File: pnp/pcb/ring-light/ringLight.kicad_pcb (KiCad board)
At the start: 2 copper layers, 40 x 50.2 mm, 33 parts, among them J1 Connector Top, J2 Connector Bot

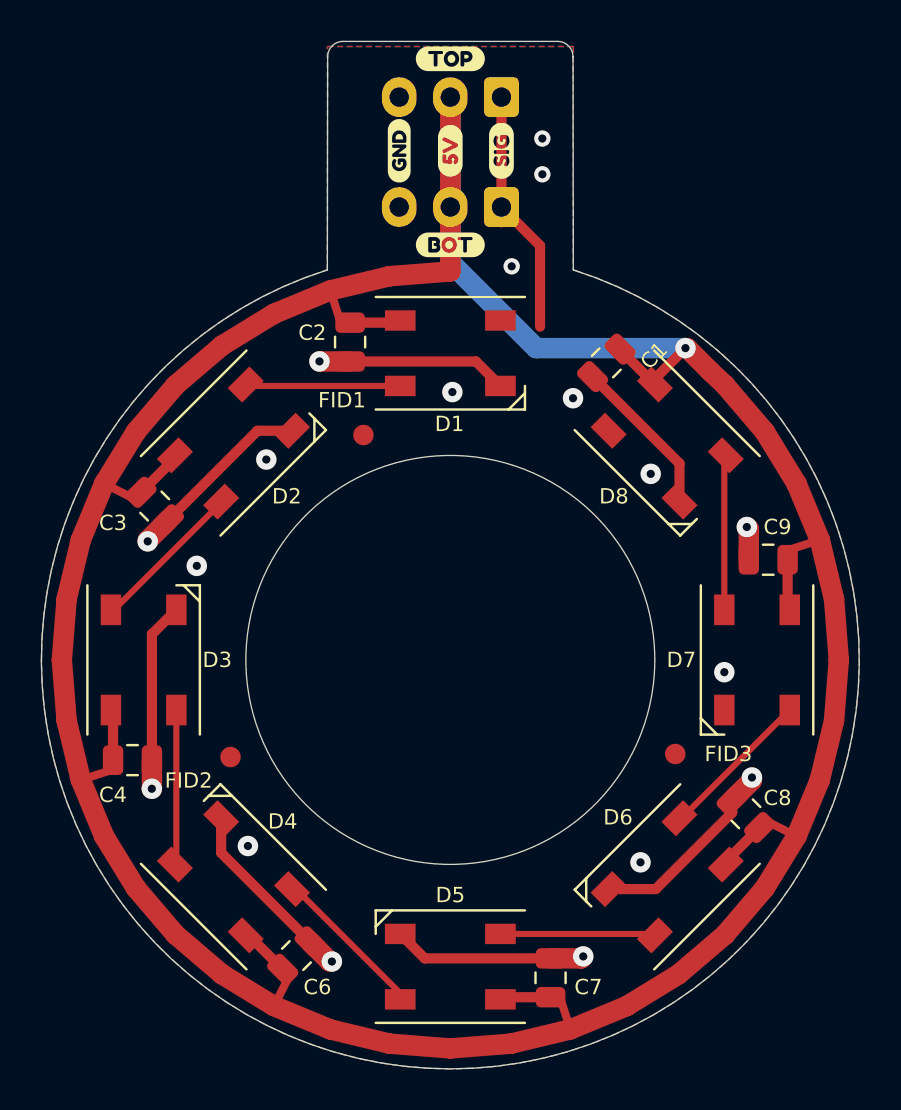
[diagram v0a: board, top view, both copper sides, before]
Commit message: reverts ring light to original design with level shifters
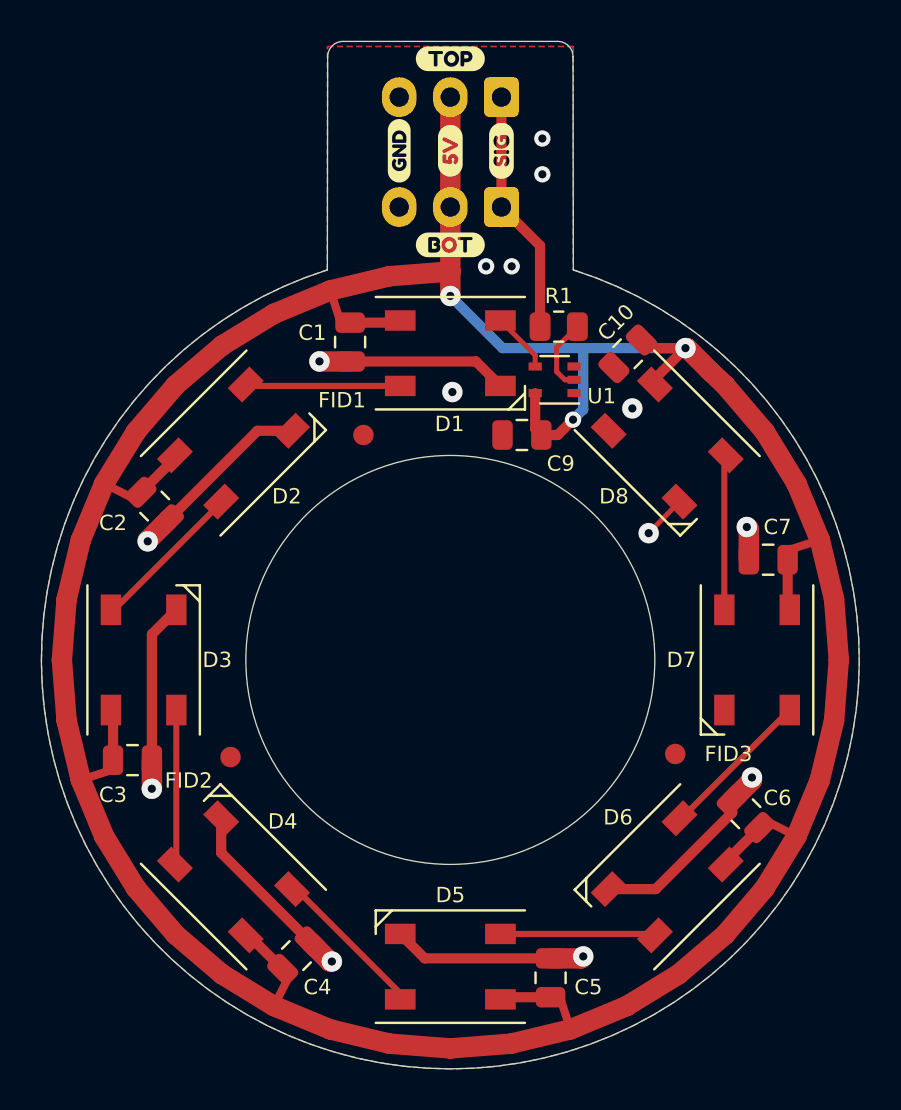
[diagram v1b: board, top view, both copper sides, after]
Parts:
- added C10: 100nF, Capacitor_SMD:C_0805_2012Metric, F.Cu at (158.7, 85.0)
- added R1: 330R, Resistor_SMD:R_0805_2012Metric, F.Cu at (155.3, 83.7)
- added U1: 74AHCT1G32, Package_TO_SOT_SMD:SOT-353_SC-70-5, F.Cu at (155.1, 86.3)
- J1: value Connector Top -> Connector Vertical
- J2: value Connector Bot -> Connector Horizontal
- moved C9 5.43 mm to (153.5, 89.0), turned to 180 degrees
- renumbered C2 to C1, C3 to C2, C4 to C3, C6 to C4, C7 to C5, C8 to C6, C9 to C7, C1 to C9, G1 to LOGO
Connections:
- D1 pad 4: /Data -> Data_In_5V
- J1 pad 1: /Data -> Data_In_3V3
- J2 pad 1: /Data -> Data_In_3V3
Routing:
- net Data_In_3V3: track 0.00 -> 12.8 mm
- net /Data: track 12.8 -> 0.00 mm
- net GND: track 65.9 -> 60.2 mm, vias 18 -> 14
- net Net-(R1-Pad1): track 0.00 -> 3.64 mm
- net Data_In_5V: track 0.00 -> 2.95 mm
- net +5V: track 173.6 -> 173.7 mm, vias 1 -> 3

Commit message: ring light: update pcb from sch (only text fields changed)
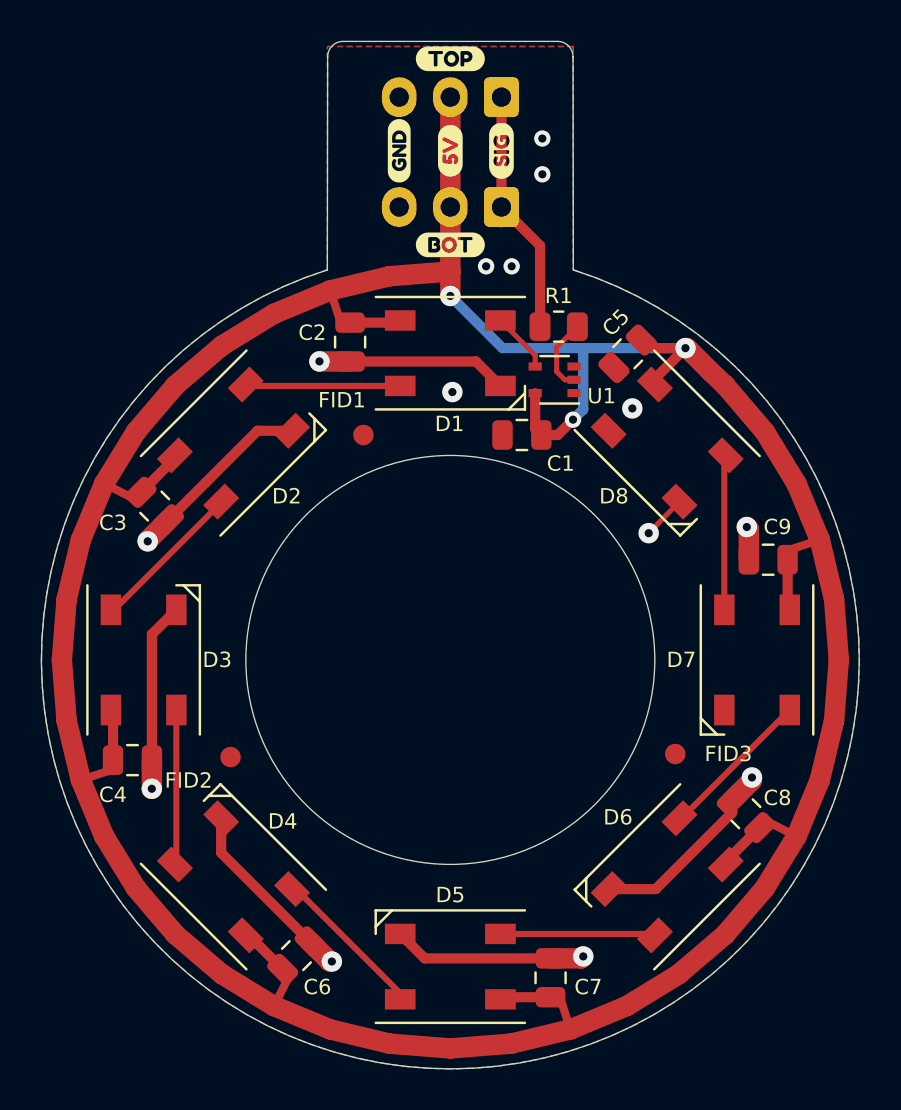
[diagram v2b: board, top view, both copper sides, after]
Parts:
- J1: value Connector Vertical -> Connector Top
- J2: value Connector Horizontal -> Connector Bot
- renumbered C9 to C1, C1 to C2, C2 to C3, C3 to C4, C10 to C5, C4 to C6, C5 to C7, C6 to C8, C7 to C9
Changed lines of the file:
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@@
     (property "Sheetname" "")
     (attr smd)
-    (fp_text reference "C1" (at -0.454414 1.848496 180) (layer "F.SilkS")
+    (fp_text reference "C2" (at -0.454414 1.848496 180) (layer "F.SilkS")
       (effects (font (size 0.75 0.75) (thickness 0.12)))
     )
@@
     (property "Sheetname" "")
     (attr smd)
-    (fp_text reference "C3" (at -0.954414 1.698496) (layer "F.SilkS")
+    (fp_text reference "C4" (at -0.954414 1.698496) (layer "F.SilkS")
       (effects (font (size 0.75 0.75) (thickness 0.12)))
     )
@@
     (property "Sheetname" "")
     (attr smd)
-    (fp_text reference "C5" (at -0.454414 1.848496 180) (layer "F.SilkS")
+    (fp_text reference "C7" (at -0.454414 1.848496 180) (layer "F.SilkS")
       (effects (font (size 0.75 0.75) (thickness 0.12)))
     )
@@
     (property "Sheetname" "")
     (attr smd)
-    (fp_text reference "C7" (at -0.454414 1.598496 180) (layer "F.SilkS")
+    (fp_text reference "C9" (at -0.454414 1.598496 180) (layer "F.SilkS")
       (effects (font (size 0.75 0.75) (thickness 0.12)))
     )
@@
     (property "Sheetname" "")
     (attr smd)
-    (fp_text reference "C6" (at -0.541094 1.639233 180) (layer "F.SilkS")
+    (fp_text reference "C8" (at -0.541094 1.639233 180) (layer "F.SilkS")
       (effects (font (size 0.75 0.75) (thickness 0.12)))
     )
@@
     (property "Sheetname" "")
     (attr smd)
-    (fp_text reference "C2" (at -0.859292 2.028142) (layer "F.SilkS")
+    (fp_text reference "C3" (at -0.859292 2.028142) (layer "F.SilkS")
       (effects (font (size 0.75 0.75) (thickness 0.12)))
     )
@@
     (property "Sheetname" "")
     (attr smd)
-    (fp_text reference "C4" (at -0.364317 1.81601 180) (layer "F.SilkS")
+    (fp_text reference "C6" (at -0.364317 1.81601 180) (layer "F.SilkS")
       (effects (font (size 0.75 0.75) (thickness 0.12)))
     )
@@
       (effects (font (size 0.9 0.9) (thickness 0.12)))
     )
-    (fp_text value "Connector Horizontal" (at 2.5 0) (layer "F.Fab")
+    (fp_text value "Connector Bot" (at 2.5 0) (layer "F.Fab")
       (effects (font (size 0.5 0.5) (thickness 0.1)))
     )
@@
     (property "Sheetname" "")
     (attr smd)
-    (fp_text reference "C10" (at -0.676346 1.484924 45) (layer "F.SilkS")
+    (fp_text reference "C5" (at -0.676346 1.484924 45) (layer "F.SilkS")
       (effects (font (size 0.75 0.75) (thickness 0.12)))
     )
@@
     (property "Sheetname" "")
     (attr smd)
-    (fp_text reference "C9" (at -1.9 -1.4 180) (layer "F.SilkS")
+    (fp_text reference "C1" (at -1.9 -1.4 180) (layer "F.SilkS")
       (effects (font (size 0.75 0.75) (thickness 0.12)))
     )
@@
       (effects (font (size 0.9 0.9) (thickness 0.12)) (justify mirror))
     )
-    (fp_text value "Connector Vertical" (at 2.5 0 180) (layer "B.Fab")
+    (fp_text value "Connector Top" (at 2.5 0 180) (layer "B.Fab")
       (effects (font (size 0.5 0.5) (thickness 0.1)) (justify mirror))
     )
